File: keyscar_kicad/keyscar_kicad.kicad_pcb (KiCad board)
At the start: 2 copper layers, 12.7 x 15 mm, 29 parts, among them SW1 K3-1292S-P2, SW2 K3-1292S-P2, SW5_MASTER_EXEC1 K2-6639SP-C4SC-04, SW6_SLAVE_EXEC2 K2-6639SP-C4SC-04

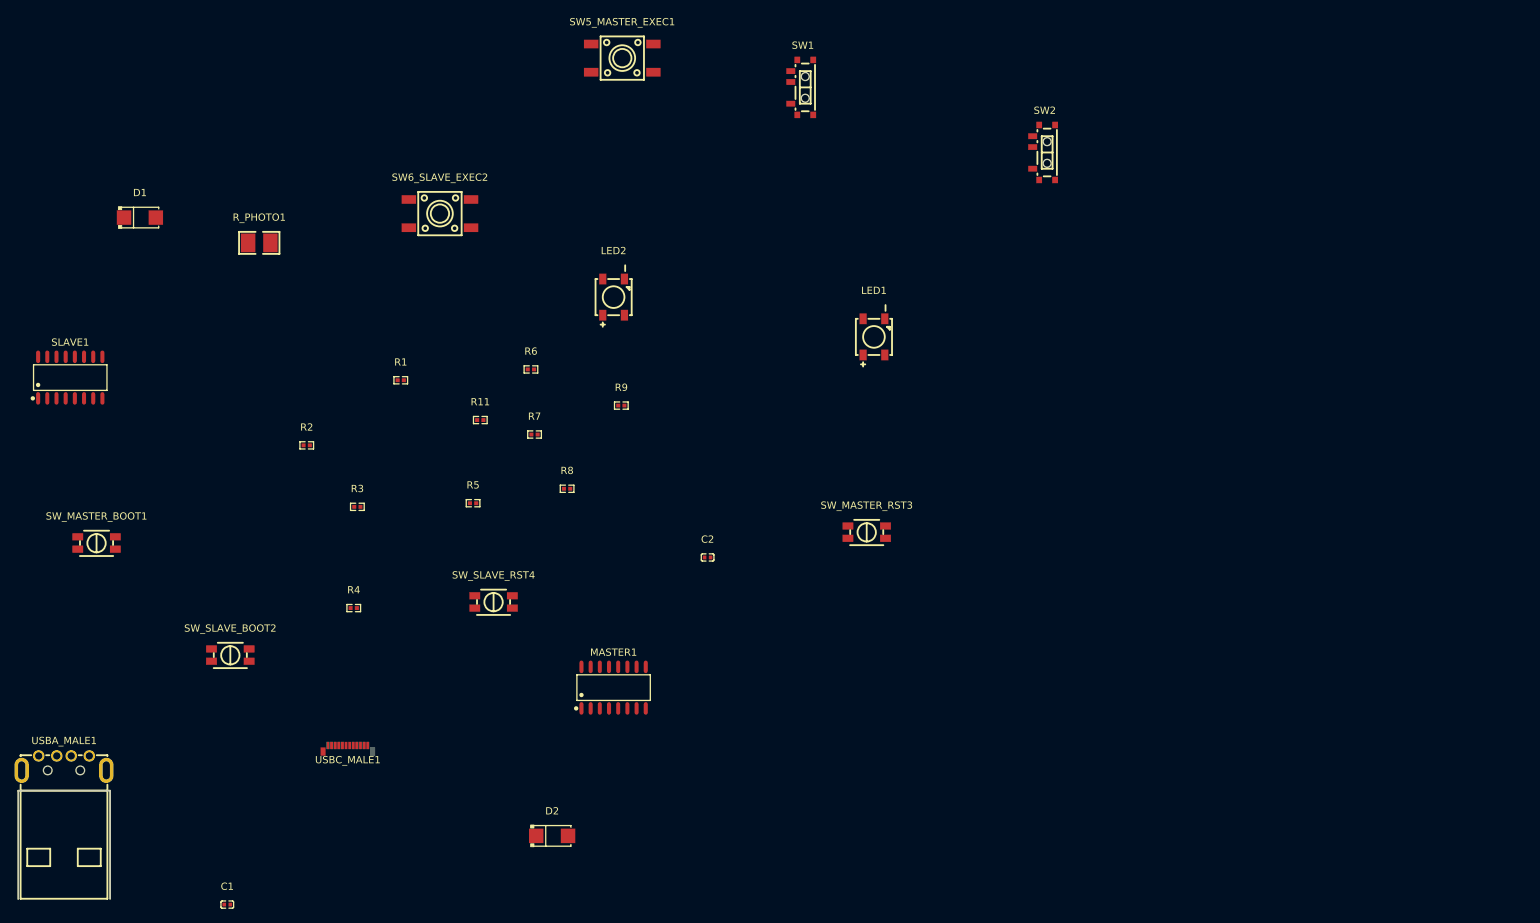
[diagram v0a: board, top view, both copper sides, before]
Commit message: Getting Started on Wiring the PCB & Substituting Parts
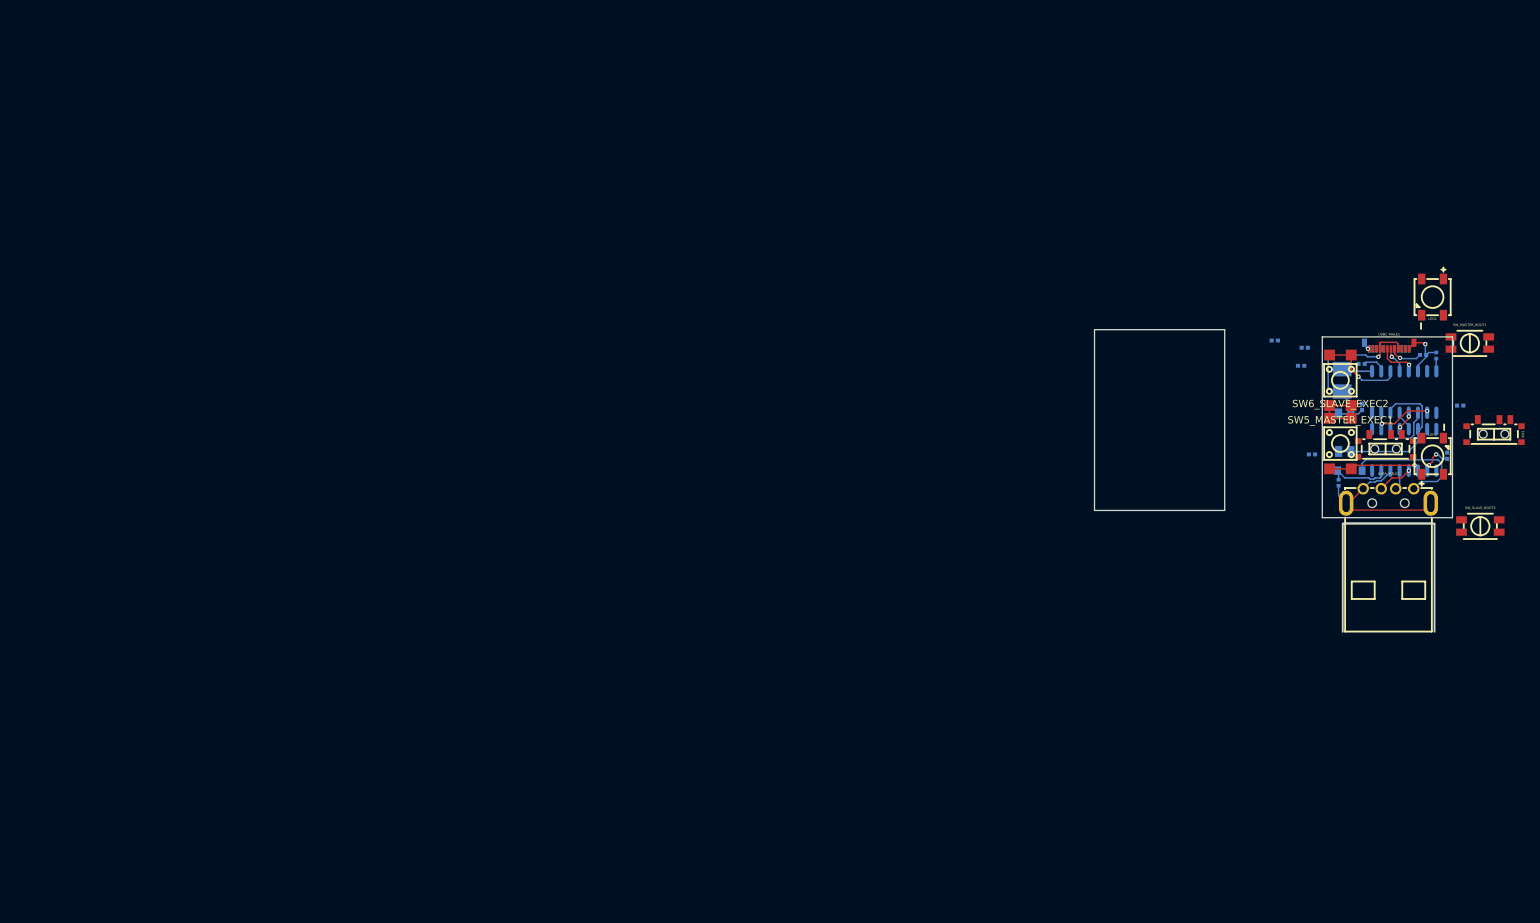
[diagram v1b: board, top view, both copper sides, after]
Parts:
- removed R3: 0402WGJ0103TCE, Library:R0402
- removed SW_SLAVE_RST4: EVQP2D02Q, Library:KEY-SMD_4P-L4.7-W3.5-P1.70-LS5.5
- C1, C2, MASTER1, R1, R11, R2, R4, R5, R6, R7, R8, R9, R_PHOTO1, SLAVE1: moved to B.Cu
- D1, D2: value SS12 -> B5817W_C8597; footprint Library:SMA_L4.3-W2.6-LS5.2-RD -> Library:SOD-123_L2.8-W1.8-LS3.7-RD; moved to B.Cu
- SW5_MASTER_EXEC1, SW6_SLAVE_EXEC2: value K2-6639SP-C4SC-04 -> TSA453G50-250; footprint Library:KEY-SMD_4P-L6.0-W6.0-P3.90-LS9.0 -> Library:KEY-SMD_4P-L4.5-W4.5-P3.00-LS7.5
- SW_CHIP_RST3: renamed from SW_MASTER_RST3; moved to B.Cu
- moved SW_MASTER_BOOT1 191.9 mm to (265.4, 74.4)
- moved USBA_MALE1 186.8 mm to (254.1, 95.5)
- moved SLAVE1 184.7 mm to (256.3, 89.1)
- moved SW_SLAVE_BOOT2 173.8 mm to (266.8, 99.7)
- moved D1 167.1 mm to (247.5, 76.0)
- moved C1 164.4 mm to (247.2, 93.7), turned to -90 degrees
- moved USBC_MALE1 154.1 mm to (254.2, 75.2), turned to 180 degrees
- moved R_PHOTO1 151.0 mm to (247.8, 79.5), turned to 90 degrees
- moved R4 142.2 mm to (250.5, 83.2), turned to -90 degrees
- moved R2 137.9 mm to (242.1, 77.5), turned to 180 degrees
- moved R5 137.2 mm to (264.1, 83.0), turned to 180 degrees
- moved R11 130.7 mm to (258.9, 76.0), turned to 180 degrees
- moved SW6_SLAVE_EXEC2 128.5 mm to (247.5, 88.2)
- moved R1 125.1 mm to (242.6, 75.0), turned to 180 degrees
- moved R8 121.8 mm to (262.2, 89.9), turned to -90 degrees
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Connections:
- R4 pad 1: V33 -> VCC
- SLAVE1 pad 6: SLAVE RST -> MASTER RST
- SW5_MASTER_EXEC1 pad 1: Net-(MASTER1-P3.4/PWM2/RXD1_/T0) -> V33
- SW5_MASTER_EXEC1 pad 4: V33 -> Net-(MASTER1-P3.4/PWM2/RXD1_/T0)
- SW6_SLAVE_EXEC2 pad 1: Net-(SLAVE1-P3.4/PWM2/RXD1_/T0) -> V33
- SW6_SLAVE_EXEC2 pad 4: V33 -> Net-(SLAVE1-P3.4/PWM2/RXD1_/T0)
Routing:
- net GND: track 0.00 -> 34.3 mm, vias 0 -> 2
- net MASTER RST: track 0.00 -> 22.5 mm
- net VCC: track 0.00 -> 19.8 mm
- net Net-(D2-A): track 0.00 -> 18.8 mm
- net Net-(SLAVE1-P3.4/PWM2/RXD1_/T0): track 0.00 -> 12.9 mm, vias 0 -> 1
- net Net-(MASTER1-P3.4/PWM2/RXD1_/T0): track 0.00 -> 12.0 mm, vias 0 -> 1
- net V33: track 0.00 -> 11.3 mm
- net Net-(D1-A): track 0.00 -> 9.83 mm, vias 0 -> 1
- net SPI MOSI: track 0.00 -> 7.79 mm
- net SPI SS: track 0.00 -> 7.77 mm, vias 0 -> 2
- net MASTERC D-: track 0.00 -> 5.32 mm, vias 0 -> 1
- net SLAVEA D+: track 0.00 -> 4.85 mm, vias 0 -> 1
- net Net-(USBC_MALE1-CC): track 0.00 -> 4.65 mm, vias 0 -> 1
- net Net-(SLAVE1-P3.3/INT1): track 0.00 -> 4.52 mm, vias 0 -> 2
- net Net-(MASTER1-P1.1/T2EX/CAP2/TIN1/VBUS2/AIN0): track 0.00 -> 4.25 mm
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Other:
- board size 12.7 x 15 mm -> 49.5 x 26 mm

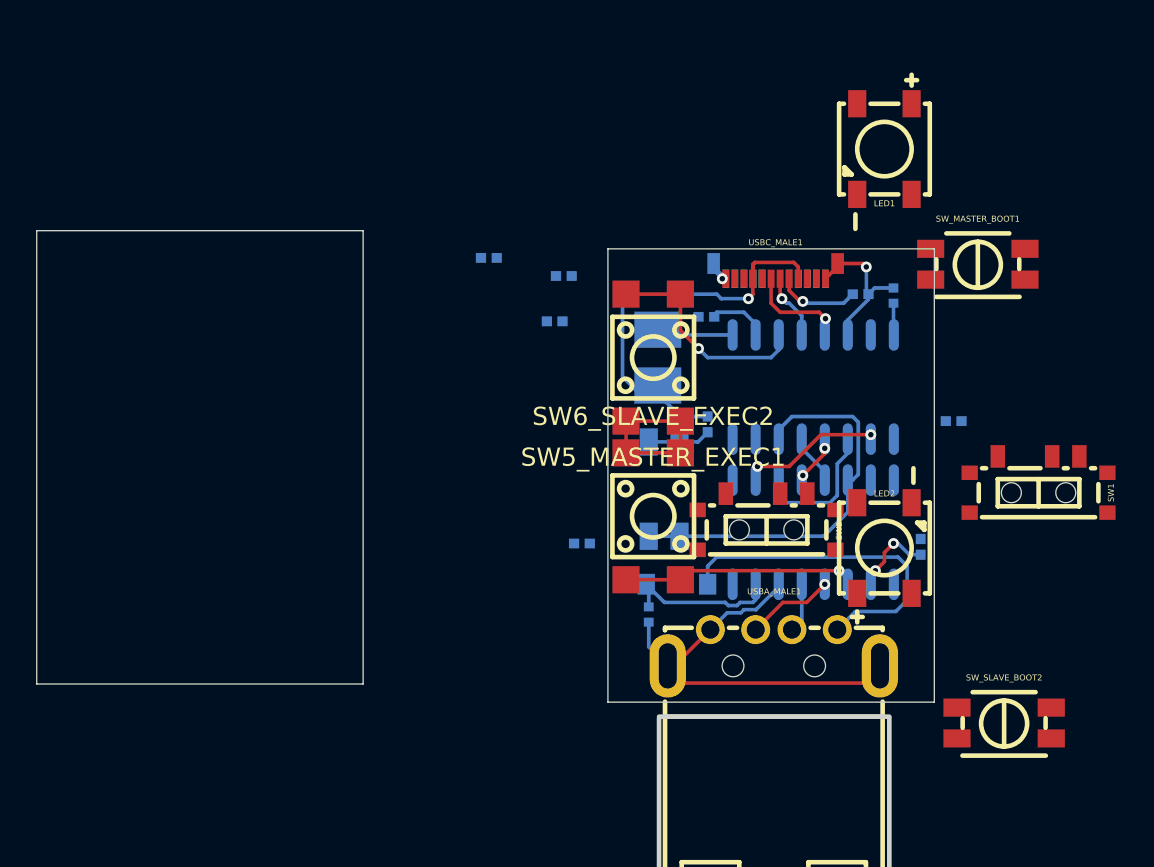
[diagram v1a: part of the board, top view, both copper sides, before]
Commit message: Wrapping up the PCB, wiring the VCC, V33, GND
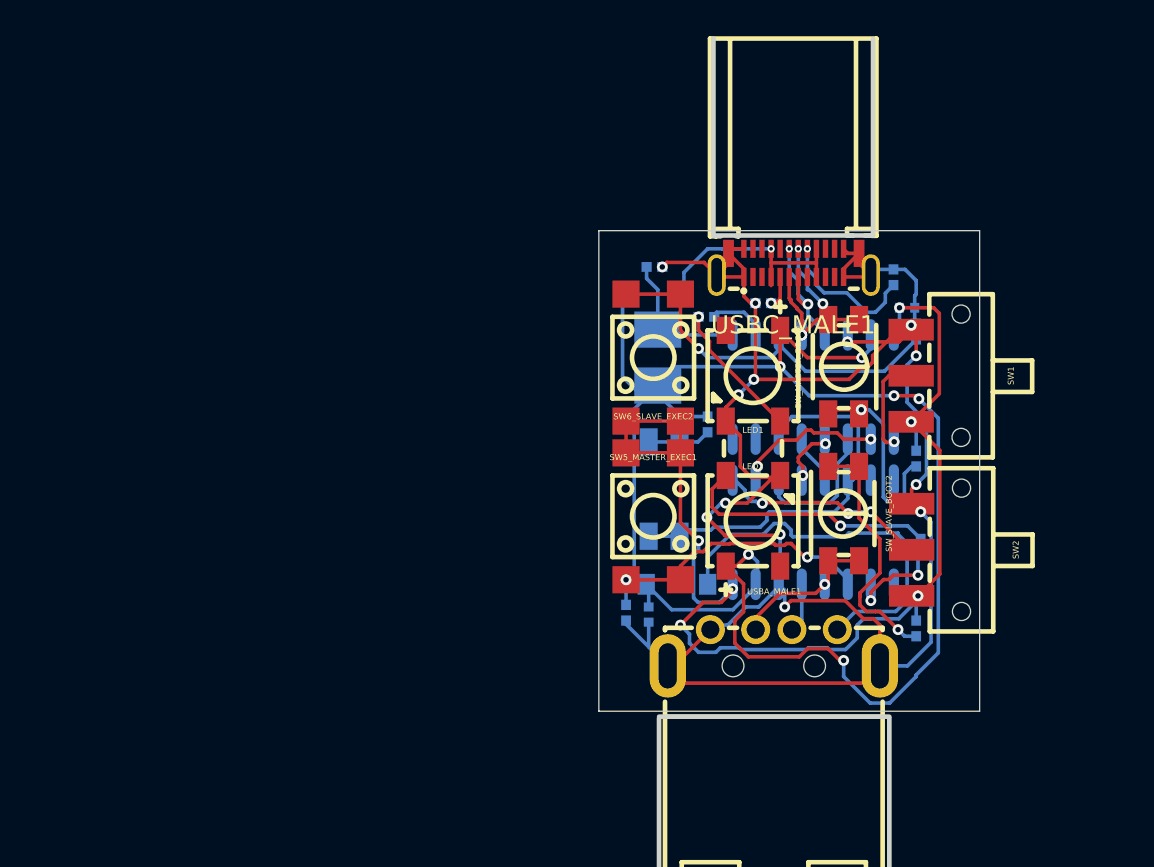
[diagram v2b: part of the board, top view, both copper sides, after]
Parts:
- added R3: 0402WGF5101TCE, Library:R0402, B.Cu at (260.8, 75.1)
- SW1, SW2: value K3-1292S-P2 -> SSSS211603; footprint Library:SW-SMD_K3-1292S-P2 -> Library:SW-SMD_SSSS211603
- USBC_MALE1: value USB_C_Plug_USB2.0 -> 918-118A2021S40003; footprint Connector_USB:USB_C_Plug_Molex_105444 -> Library:USB-C-SMD_918-118A2021S40003
- moved R2 26.2 mm to (262.0, 94.4), turned to -90 degrees
- moved R1 21.9 mm to (262.0, 85.1), turned to -90 degrees
- moved SW_SLAVE_BOOT2 14.6 mm to (258.0, 88.1), turned to -90 degrees
- moved LED1 14.5 mm to (253.0, 80.5)
- moved SW_MASTER_BOOT1 9.31 mm to (258.0, 80.0), turned to 90 degrees
- moved SW1 9.24 mm to (261.7, 80.5)
- moved R9 9.15 mm to (247.6, 74.5)
- moved SW2 8.15 mm to (261.7, 90.1)
- moved LED2 7.40 mm to (253.0, 88.5)
- moved R11 5.39 mm to (253.6, 76.5), turned to 0 degrees
- moved R5 5.35 mm to (262.0, 78.1), turned to -90 degrees
- moved R6 4.53 mm to (246.0, 93.6), turned to 90 degrees
- moved USBC_MALE1 1.36 mm to (255.3, 74.3)
- moved C2 1.01 mm to (261.5, 76.8), turned to 0 degrees
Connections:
- net Net-(D1-A) renamed USB C VBUS
- USBC_MALE1 pad A10: (no net) -> unconnected-(USBC_MALE1-SSRXN2-PadA10)
- USBC_MALE1 pad A11: (no net) -> unconnected-(USBC_MALE1-SSRXP2-PadA11)
- USBC_MALE1 pad A2: (no net) -> unconnected-(USBC_MALE1-SSTXP1-PadA2)
- USBC_MALE1 pad A3: (no net) -> unconnected-(USBC_MALE1-SSTXN1-PadA3)
- USBC_MALE1 pad A8: (no net) -> unconnected-(USBC_MALE1-SUB1-PadA8)
- USBC_MALE1 pad B10: (no net) -> unconnected-(USBC_MALE1-SSRXN1-PadB10)
- USBC_MALE1 pad B11: (no net) -> unconnected-(USBC_MALE1-SSRXP1-PadB11)
- USBC_MALE1 pad B2: (no net) -> unconnected-(USBC_MALE1-SSTXP2-PadB2)
- USBC_MALE1 pad B3: (no net) -> unconnected-(USBC_MALE1-SSTXN2-PadB3)
- USBC_MALE1 pad B5: USB C VCONN -> Net-(USBC_MALE1-CC2)
- USBC_MALE1 pad B8: (no net) -> unconnected-(USBC_MALE1-SUB2-PadB8)
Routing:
- net GND: track 34.3 -> 121.1 mm, vias 2 -> 13
- net VCC: track 19.8 -> 92.9 mm, vias 0 -> 6
- net V33: track 11.3 -> 65.4 mm, vias 0 -> 6
- net Net-(LED2-DIN): track 0.00 -> 14.3 mm, vias 0 -> 1
- net Net-(R2-Pad2): track 0.00 -> 14.1 mm, vias 0 -> 1
- net Net-(SLAVE1-P3.2/TXD1_/INT0/VBUS1/AIN3): track 0.00 -> 11.8 mm, vias 0 -> 3
- net Net-(R1-Pad2): track 0.00 -> 11.2 mm, vias 0 -> 1
- net Net-(MASTER1-P3.4/PWM2/RXD1_/T0): track 12.0 -> 21.5 mm
- net MASTERC D+: track 3.33 -> 11.7 mm, vias 1 -> 4
- net Net-(USBC_MALE1-CC2): track 0.00 -> 7.99 mm, vias 0 -> 1
- net Net-(LED1-DIN): track 0.00 -> 7.61 mm, vias 0 -> 1
- net Net-(MASTER1-P3.2/TXD1_/INT0/VBUS1/AIN3): track 0.00 -> 6.02 mm, vias 0 -> 1
- net Net-(SLAVE1-P3.4/PWM2/RXD1_/T0): track 12.9 -> 17.0 mm, vias 1 -> 2
- net Net-(MASTER1-P1.1/T2EX/CAP2/TIN1/VBUS2/AIN0): track 4.25 -> 7.96 mm
- net SLAVEA D+: track 4.85 -> 8.31 mm
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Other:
- board size 49.5 x 26 mm -> 21 x 26.5 mm

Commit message: medium commit
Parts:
- moved R9 0.75 mm to (247.6, 73.8)
- moved R3 0.63 mm to (260.8, 74.4)
- moved C2 0.50 mm to (261.5, 76.2)
- moved D1 0.50 mm to (247.5, 75.5)
- moved C1 0.48 mm to (247.0, 94.1)
- moved R6 0.25 mm to (245.8, 93.6)
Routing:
- net GND: track 121.1 -> 123.7 mm
- net VCC: track 92.9 -> 94.0 mm
- net Net-(MASTER1-P1.1/T2EX/CAP2/TIN1/VBUS2/AIN0): track 7.96 -> 8.71 mm
- net V33: track 65.4 -> 66.2 mm
- net Net-(USBC_MALE1-CC2): track 7.99 -> 8.63 mm
- net USB C VBUS: track 11.9 -> 11.4 mm
- net MASTERC D+: vias 4 -> 3
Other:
- board size 21 x 26.5 mm -> 21 x 26.8 mm
